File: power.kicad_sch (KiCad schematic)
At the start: 12 parts, among them U3 LMZ21701SILR

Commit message: crystals and drivers
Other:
- note added: "Make the voltage tunable between 3.6 and 2.4 V (manually)"
- note added: "https://lowpowerlab.com/forum/general-topics/ws2812b-rgb-led-measurements/"
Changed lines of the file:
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@@
     (stroke (width 0) (type default))
+  )
+  (text "https://lowpowerlab.com/forum/general-topics/ws2812b-rgb-led-measurements/"
+    (at 104.14 110.49 0)
+    (effects (font (size 1.27 1.27)) (justify left bottom) (href "https://lowpowerlab.com/forum/general-topics/ws2812b-rgb-led-measurements/"))
+  )
+  (text "Make the voltage tunable between 3.6 and 2.4 V (manually)"
+    (at 104.14 106.045 0)
+    (effects (font (size 1.27 1.27)) (justify left bottom))
   )
   (global_label "VDD_WS2812B" (shape input) (at 97.79 86.36 90) (fields_autoplaced)

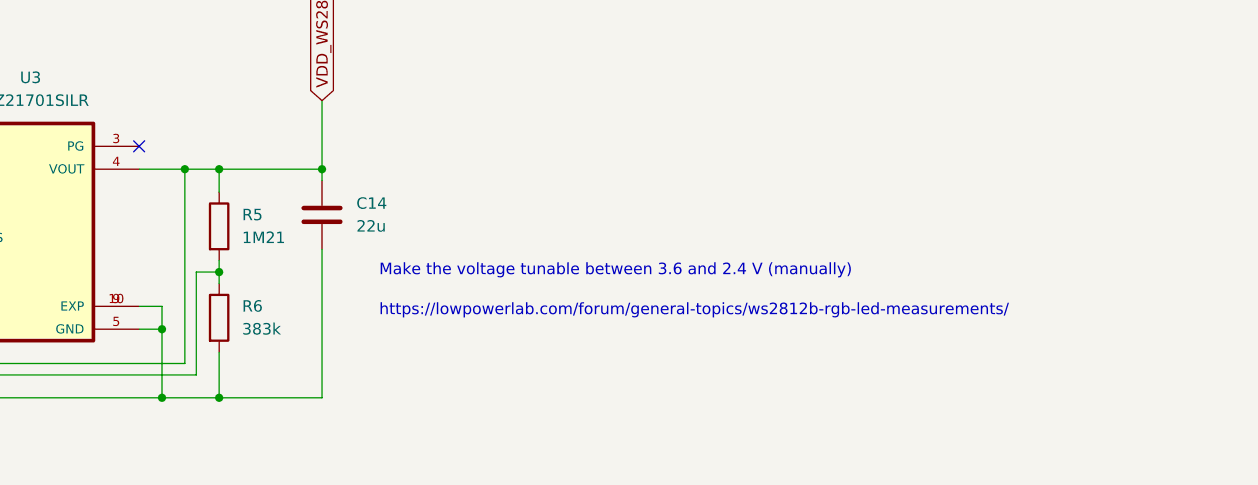
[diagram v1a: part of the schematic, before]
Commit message: more connectors and USB
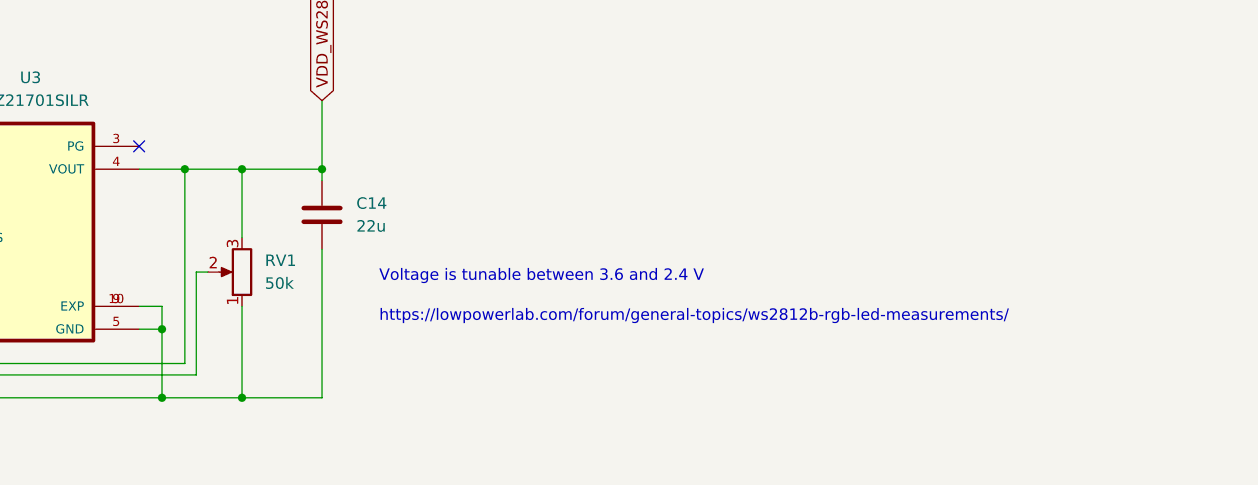
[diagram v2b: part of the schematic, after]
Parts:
- removed R5: 1M21, Resistor_SMD:R_0402_1005Metric, symbol Device:R
- removed R6: 383k, Resistor_SMD:R_0402_1005Metric, symbol Device:R
- added RV1: 50k, Potentiometer_THT:Potentiometer_Bourns_3296W_Vertical, symbol Device:R_Potentiometer
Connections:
- net GND: now also RV1.1
- net VDD_WS2812B: now also RV1.3
- net at U3.2 (FB): now also RV1.2
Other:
- note added: "Voltage is tunable between 3.6 and 2.4 V"
- note removed: "Make the voltage tunable between 3.6 and 2.4 V (manually)"
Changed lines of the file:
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@@
   (junction (at 30.48 119.38) (diameter 0) (color 0 0 0 0)
   )
-  (junction (at 86.36 119.38) (diameter 0) (color 0 0 0 0)
-  )
   (junction (at 86.36 62.23) (diameter 0) (color 0 0 0 0)
   )
+  (junction (at 88.9 119.38) (diameter 0) (color 0 0 0 0)
+  )
   (junction (at 30.48 99.06) (diameter 0) (color 0 0 0 0)
   )
@@
   (junction (at 97.79 93.98) (diameter 0) (color 0 0 0 0)
   )
-  (junction (at 86.36 105.41) (diameter 0) (color 0 0 0 0)
-  )
   (junction (at 82.55 93.98) (diameter 0) (color 0 0 0 0)
   )
-  (junction (at 86.36 93.98) (diameter 0) (color 0 0 0 0)
+  (junction (at 88.9 93.98) (diameter 0) (color 0 0 0 0)
   )
   (junction (at 80.01 54.61) (diameter 0) (color 0 0 0 0)
@@
   (no_connect (at 77.47 34.29))
   (no_connect (at 77.47 91.44))
+  (wire (pts (xy 88.9 119.38) (xy 97.79 119.38))
+    (stroke (width 0) (type default))
+  )
   (wire (pts (xy 30.48 99.06) (xy 30.48 104.14))
     (stroke (width 0) (type default))
@@
     (stroke (width 0) (type default))
   )
-  (wire (pts (xy 86.36 105.41) (xy 83.82 105.41))
-    (stroke (width 0) (type default))
-  )
   (wire (pts (xy 86.36 57.15) (xy 86.36 62.23))
     (stroke (width 0) (type default))
@@
     (stroke (width 0) (type default))
   )
-  (wire (pts (xy 86.36 119.38) (xy 80.01 119.38))
-    (stroke (width 0) (type default))
-  )
   (wire (pts (xy 30.48 41.91) (xy 30.48 46.99))
     (stroke (width 0) (type default))
@@
     (stroke (width 0) (type default))
   )
-  (wire (pts (xy 86.36 104.14) (xy 86.36 105.41))
-    (stroke (width 0) (type default))
-  )
   (wire (pts (xy 77.47 36.83) (xy 82.55 36.83))
     (stroke (width 0) (type default))
@@
     (stroke (width 0) (type default))
   )
-  (wire (pts (xy 86.36 93.98) (xy 86.36 96.52))
+  (wire (pts (xy 88.9 109.22) (xy 88.9 119.38))
     (stroke (width 0) (type default))
   )
@@
     (stroke (width 0) (type default))
   )
-  (wire (pts (xy 86.36 114.3) (xy 86.36 119.38))
-    (stroke (width 0) (type default))
-  )
   (wire (pts (xy 40.64 39.37) (xy 40.64 46.99))
     (stroke (width 0) (type default))
@@
     (stroke (width 0) (type default))
   )
+  (wire (pts (xy 88.9 93.98) (xy 88.9 101.6))
+    (stroke (width 0) (type default))
+  )
   (wire (pts (xy 86.36 46.99) (xy 86.36 48.26))
     (stroke (width 0) (type default))
   )
-  (wire (pts (xy 86.36 105.41) (xy 86.36 106.68))
-    (stroke (width 0) (type default))
-  )
   (wire (pts (xy 86.36 48.26) (xy 86.36 49.53))
     (stroke (width 0) (type default))
@@
     (stroke (width 0) (type default))
   )
+  (wire (pts (xy 83.82 105.41) (xy 85.09 105.41))
+    (stroke (width 0) (type default))
+  )
   (wire (pts (xy 30.48 29.21) (xy 30.48 34.29))
     (stroke (width 0) (type default))
   )
-  (wire (pts (xy 86.36 93.98) (xy 97.79 93.98))
+  (wire (pts (xy 88.9 93.98) (xy 97.79 93.98))
+    (stroke (width 0) (type default))
+  )
+  (wire (pts (xy 82.55 93.98) (xy 88.9 93.98))
     (stroke (width 0) (type default))
   )
@@
     (stroke (width 0) (type default))
   )
-  (wire (pts (xy 97.79 119.38) (xy 86.36 119.38))
+  (wire (pts (xy 80.01 119.38) (xy 88.9 119.38))
     (stroke (width 0) (type default))
   )
@@
     (stroke (width 0) (type default))
   )
-  (wire (pts (xy 82.55 93.98) (xy 86.36 93.98))
-    (stroke (width 0) (type default))
-  )
   (wire (pts (xy 83.82 105.41) (xy 83.82 116.84))
     (stroke (width 0) (type default))
@@
   )
   (text "https://lowpowerlab.com/forum/general-topics/ws2812b-rgb-led-measurements/"
-    (at 104.14 110.49 0)
+    (at 104.14 111.125 0)
     (effects (font (size 1.27 1.27)) (justify left bottom) (href "https://lowpowerlab.com/forum/general-topics/ws2812b-rgb-led-measurements/"))
   )
-  (text "Make the voltage tunable between 3.6 and 2.4 V (manually)"
-    (at 104.14 106.045 0)
+  (text "Voltage is tunable between 3.6 and 2.4 V" (at 104.14 106.68 0)
     (effects (font (size 1.27 1.27)) (justify left bottom))
   )
@@
     )
   )
-  (symbol (lib_id "Device:R") (at 86.36 100.33 0) (unit 1)
-    (in_bom yes) (on_board yes) (dnp no) (fields_autoplaced)
-    (property "Reference" "R5" (at 88.9 99.06 0)
-      (effects (font (size 1.27 1.27)) (justify left))
-    )
-    (property "Value" "1M21" (at 88.9 101.6 0)
-      (effects (font (size 1.27 1.27)) (justify left))
-    )
-    (property "Footprint" "Resistor_SMD:R_0402_1005Metric" (at 84.582 100.33 90)
-      (effects (font (size 1.27 1.27)) hide)
-    )
-    (property "Datasheet" "~" (at 86.36 100.33 0)
-      (effects (font (size 1.27 1.27)) hide)
-    )
-    (pin "1")
-    (pin "2")
-    (instances
-      (project "trackinator"
-        (path "/21f69d4f-5d5e-42f8-b3db-8d41c47386dd"
-          (reference "R5") (unit 1)
-        )
-        (path "/21f69d4f-5d5e-42f8-b3db-8d41c47386dd/e63bfbc8-53d7-4fc8-9d4c-c9a46bf54919"
-          (reference "R11") (unit 1)
+  (symbol (lib_id "Device:R_Potentiometer") (at 88.9 105.41 180) (unit 1)
+    (in_bom yes) (on_board yes) (dnp no) (fields_autoplaced)
+    (property "Reference" "RV1" (at 91.44 104.14 0)
+      (effects (font (size 1.27 1.27)) (justify right))
+    )
+    (property "Value" "50k" (at 91.44 106.68 0)
+      (effects (font (size 1.27 1.27)) (justify right))
+    )
+    (property "Footprint" "Potentiometer_THT:Potentiometer_Bourns_3296W_Vertical" (at 88.9 105.41 0)
+      (effects (font (size 1.27 1.27)) hide)
+    )
+    (property "Datasheet" "~" (at 88.9 105.41 0)
+      (effects (font (size 1.27 1.27)) hide)
+    )
+    (pin "1")
+    (pin "2")
+    (pin "3")
+    (instances
+      (project "trackinator"
+        (path "/21f69d4f-5d5e-42f8-b3db-8d41c47386dd/e63bfbc8-53d7-4fc8-9d4c-c9a46bf54919"
+          (reference "RV1") (unit 1)
         )
       )
@@
         )
       )
-    )
-  )
-  (symbol (lib_id "Device:R") (at 86.36 110.49 0) (unit 1)
-    (in_bom yes) (on_board yes) (dnp no) (fields_autoplaced)
-    (property "Reference" "R6" (at 88.9 109.22 0)
-      (effects (font (size 1.27 1.27)) (justify left))
-    )
-    (property "Value" "383k" (at 88.9 111.76 0)
-      (effects (font (size 1.27 1.27)) (justify left))
-    )
-    (property "Footprint" "Resistor_SMD:R_0402_1005Metric" (at 84.582 110.49 90)
-      (effects (font (size 1.27 1.27)) hide)
-    )
-    (property "Datasheet" "~" (at 86.36 110.49 0)
-      (effects (font (size 1.27 1.27)) hide)
-    )
-    (pin "1")
-    (pin "2")
-    (instances
-      (project "trackinator"
-        (path "/21f69d4f-5d5e-42f8-b3db-8d41c47386dd"
-          (reference "R6") (unit 1)
-        )
-        (path "/21f69d4f-5d5e-42f8-b3db-8d41c47386dd/e63bfbc8-53d7-4fc8-9d4c-c9a46bf54919"
-          (reference "R26") (unit 1)
-        )
-      )

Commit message: savin' my work!
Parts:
- added C1 (x4): 10u, Capacitor_SMD:C_0603_1608Metric, symbol Device:C
- added R5 (x4): tbd, Resistor_SMD:R_0402_1005Metric, symbol Device:R
- added U14, U15: ADP125ARHZ-R7, easyeda2kicad:MSOP-8_L3.0-W3.0-P0.65-LS4.9-BL-EP, symbol easyeda2kicad:ADP125ARHZ-R7
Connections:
- net +3V3: now also C1.2, C1.2, U14.5 (EN), U14.7 (VIN), U14.8 (VIN), U15.5 (EN), U15.7 (VIN), U15.8 (VIN)
- net GND: now also C1.1, C1.1, C1.1, C1.1, R5.2, R5.2, U14.4 (GND), U14.9 (PAD), U15.4 (GND), U15.9 (PAD)
- new net: R5.1, R5.2, U15.3 (ADJ)
- new net: R5.1, R5.2, U14.3 (ADJ)
- new net VCC_1V2: C1.2, R5.1, U15.1 (VOUT), U15.2 (VOUT)
- new net VCC_2V8: C1.2, R5.1, U14.1 (VOUT), U14.2 (VOUT)
- no-connect marks 2 -> 4
